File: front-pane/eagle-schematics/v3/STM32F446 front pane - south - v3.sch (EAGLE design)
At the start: 435 parts, among them IC1 NEOPIXEL-TLC59731DR, IC10 NEOPIXEL-TLC59731DR, IC11 NEOPIXEL-TLC59731DR, IC12 NEOPIXEL-TLC59731DR, IC13 NEOPIXEL-TLC59731DR, IC14 NEOPIXEL-TLC59731DR, IC15 NEOPIXEL-TLC59731DR, IC16 NEOPIXEL-TLC59731DR, IC17 NEOPIXEL-TLC59731DR, IC18 NEOPIXEL-TLC59731DR, IC19 NEOPIXEL-TLC59731DR, IC2 NEOPIXEL-TLC59731DR, IC20 NEOPIXEL-TLC59731DR, IC21 NEOPIXEL-TLC59731DR, IC22 NEOPIXEL-TLC59731DR, IC23 NEOPIXEL-TLC59731DR, IC24 NEOPIXEL-TLC59731DR, IC25 NEOPIXEL-TLC59731DR, IC26 NEOPIXEL-TLC59731DR, IC27 NEOPIXEL-TLC59731DR, IC28 NEOPIXEL-TLC59731DR, IC29 NEOPIXEL-TLC59731DR, IC3 NEOPIXEL-TLC59731DR, IC30 NEOPIXEL-TLC59731DR, IC31 NEOPIXEL-TLC59731DR, IC32 NEOPIXEL-TLC59731DR, IC33 NEOPIXEL-TLC59731DR, IC4 NEOPIXEL-TLC59731DR, IC5 NEOPIXEL-TLC59731DR, IC6 NEOPIXEL-TLC59731DR, IC7 NEOPIXEL-TLC59731DR, IC8 NEOPIXEL-TLC59731DR, IC9 NEOPIXEL-TLC59731DR, SW1 B3F-1000, SW10 B3F-1000, SW2 B3F-1000, SW3 B3F-1000, SW4 B3F-1000, SW5 B3F-1000, SW6 B3F-1000, SW7 B3F-1000, SW8 B3F-1000, SW9 B3F-1000

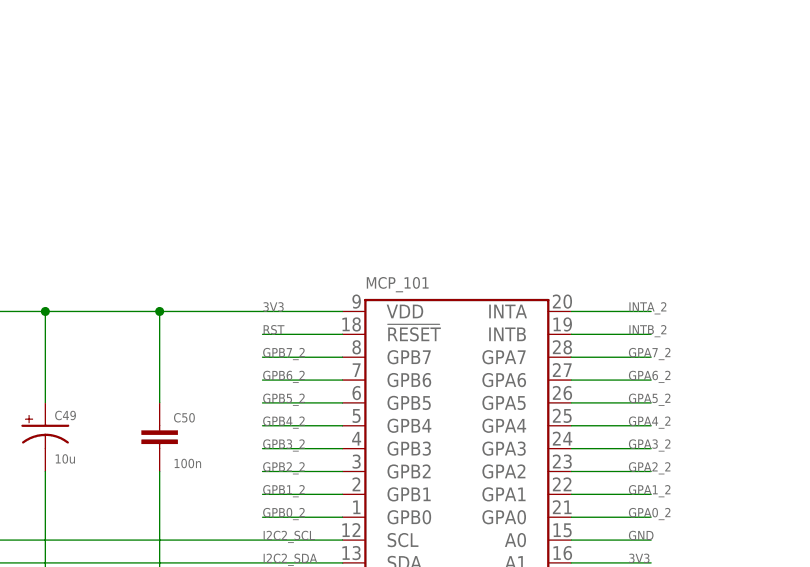
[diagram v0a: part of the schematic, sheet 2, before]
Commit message: Fixed bug with MCP_XXX name
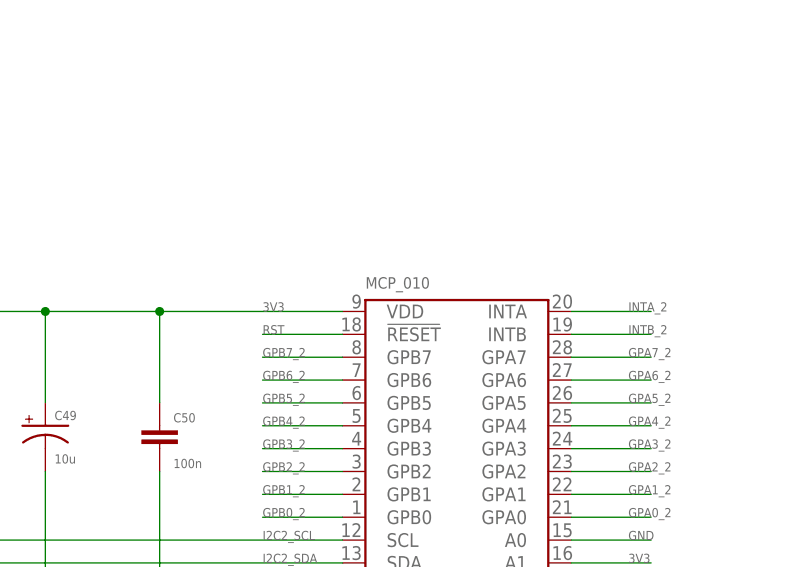
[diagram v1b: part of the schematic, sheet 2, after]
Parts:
- renumbered MCP_101 to MCP_010
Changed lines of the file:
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@@
 <part name="C75" library="stock-perso" deviceset="PASSIF-CAP" device="-0805" value="100n"/>
 <part name="C79" library="stock-perso" deviceset="PASSIF-CPOL-US" device="2917" value="10u"/>
-<part name="MCP_101" library="a_ranger_work" deviceset="MCP23017" device=""/>
+<part name="MCP_010" library="a_ranger_work" deviceset="MCP23017" device=""/>
 <part name="C49" library="stock-perso" deviceset="PASSIF-CPOL-US" device="2917" value="10u"/>
 <part name="C50" library="stock-perso" deviceset="PASSIF-CAP" device="-0805" value="100n"/>
@@
 <attribute name="VALUE" x="368.046" y="275.209" size="1.778" layer="96"/>
 </instance>
-<instance part="MCP_101" gate="G$1" x="-78.74" y="189.23" smashed="yes">
+<instance part="MCP_010" gate="G$1" x="-78.74" y="189.23" smashed="yes">
 <attribute name="NAME" x="-88.9" y="205.74" size="1.27" layer="95" ratio="12"/>
 <attribute name="VALUE" x="-88.9" y="168.91" size="1.27" layer="96" ratio="12"/>
@@
 </segment>
 <segment>
-<pinref part="MCP_101" gate="G$1" pin="VSS"/>
+<pinref part="MCP_010" gate="G$1" pin="VSS"/>
 <label x="-100.33" y="172.72" size="1.016" layer="95"/>
 <pinref part="C49" gate="G$1" pin="-"/>
@@
 <segment>
 <wire x1="-66.04" y1="172.72" x2="-57.15" y2="172.72" width="0.1524" layer="91"/>
-<pinref part="MCP_101" gate="G$1" pin="A2"/>
+<pinref part="MCP_010" gate="G$1" pin="A2"/>
 <label x="-59.69" y="172.72" size="1.016" layer="95"/>
 </segment>
 <segment>
 <wire x1="-66.04" y1="177.8" x2="-57.15" y2="177.8" width="0.1524" layer="91"/>
-<pinref part="MCP_101" gate="G$1" pin="A0"/>
+<pinref part="MCP_010" gate="G$1" pin="A0"/>
 <label x="-59.69" y="177.8" size="1.016" layer="95"/>
 </segment>
@@
 </segment>
 <segment>
-<pinref part="MCP_101" gate="G$1" pin="VDD"/>
+<pinref part="MCP_010" gate="G$1" pin="VDD"/>
 <label x="-100.33" y="203.2" size="1.016" layer="95"/>
 <wire x1="-91.44" y1="203.2" x2="-111.76" y2="203.2" width="0.1524" layer="91"/>
@@
 <segment>
 <wire x1="-66.04" y1="175.26" x2="-57.15" y2="175.26" width="0.1524" layer="91"/>
-<pinref part="MCP_101" gate="G$1" pin="A1"/>
+<pinref part="MCP_010" gate="G$1" pin="A1"/>
 <label x="-59.69" y="175.26" size="1.016" layer="95"/>
 </segment>
@@
 <segment>
 <wire x1="-100.33" y1="200.66" x2="-91.44" y2="200.66" width="0.1524" layer="91"/>
-<pinref part="MCP_101" gate="G$1" pin="!RESET"/>
+<pinref part="MCP_010" gate="G$1" pin="!RESET"/>
 <label x="-100.33" y="200.66" size="1.016" layer="95"/>
 </segment>
@@
 <segment>
 <wire x1="-100.33" y1="198.12" x2="-91.44" y2="198.12" width="0.1524" layer="91"/>
-<pinref part="MCP_101" gate="G$1" pin="GPB7"/>
+<pinref part="MCP_010" gate="G$1" pin="GPB7"/>
 <label x="-100.33" y="198.12" size="1.016" layer="95"/>
 </segment>
@@
 <segment>
 <wire x1="-100.33" y1="195.58" x2="-91.44" y2="195.58" width="0.1524" layer="91"/>
-<pinref part="MCP_101" gate="G$1" pin="GPB6"/>
+<pinref part="MCP_010" gate="G$1" pin="GPB6"/>
 <label x="-100.33" y="195.58" size="1.016" layer="95"/>
 </segment>
@@
 <segment>
 <wire x1="-100.33" y1="193.04" x2="-91.44" y2="193.04" width="0.1524" layer="91"/>
-<pinref part="MCP_101" gate="G$1" pin="GPB5"/>
+<pinref part="MCP_010" gate="G$1" pin="GPB5"/>
 <label x="-100.33" y="193.04" size="1.016" layer="95"/>
 </segment>
@@
 <segment>
 <wire x1="-100.33" y1="190.5" x2="-91.44" y2="190.5" width="0.1524" layer="91"/>
-<pinref part="MCP_101" gate="G$1" pin="GPB4"/>
+<pinref part="MCP_010" gate="G$1" pin="GPB4"/>
 <label x="-100.33" y="190.5" size="1.016" layer="95"/>
 </segment>
@@
 <segment>
 <wire x1="-100.33" y1="187.96" x2="-91.44" y2="187.96" width="0.1524" layer="91"/>
-<pinref part="MCP_101" gate="G$1" pin="GPB3"/>
+<pinref part="MCP_010" gate="G$1" pin="GPB3"/>
 <label x="-100.33" y="187.96" size="1.016" layer="95"/>
 </segment>
@@
 <segment>
 <wire x1="-100.33" y1="185.42" x2="-91.44" y2="185.42" width="0.1524" layer="91"/>
-<pinref part="MCP_101" gate="G$1" pin="GPB2"/>
+<pinref part="MCP_010" gate="G$1" pin="GPB2"/>
 <label x="-100.33" y="185.42" size="1.016" layer="95"/>
 </segment>
@@
 <segment>
 <wire x1="-100.33" y1="182.88" x2="-91.44" y2="182.88" width="0.1524" layer="91"/>
-<pinref part="MCP_101" gate="G$1" pin="GPB1"/>
+<pinref part="MCP_010" gate="G$1" pin="GPB1"/>
 <label x="-100.33" y="182.88" size="1.016" layer="95"/>
 </segment>
@@
 <segment>
 <wire x1="-100.33" y1="180.34" x2="-91.44" y2="180.34" width="0.1524" layer="91"/>
-<pinref part="MCP_101" gate="G$1" pin="GPB0"/>
+<pinref part="MCP_010" gate="G$1" pin="GPB0"/>
 <label x="-100.33" y="180.34" size="1.016" layer="95"/>
 </segment>
@@
 <segment>
 <wire x1="-66.04" y1="180.34" x2="-57.15" y2="180.34" width="0.1524" layer="91"/>
-<pinref part="MCP_101" gate="G$1" pin="GPA0"/>
+<pinref part="MCP_010" gate="G$1" pin="GPA0"/>
 <label x="-59.69" y="180.34" size="1.016" layer="95"/>
 </segment>
@@
 <segment>
 <wire x1="-66.04" y1="182.88" x2="-57.15" y2="182.88" width="0.1524" layer="91"/>
-<pinref part="MCP_101" gate="G$1" pin="GPA1"/>
+<pinref part="MCP_010" gate="G$1" pin="GPA1"/>
 <label x="-59.69" y="182.88" size="1.016" layer="95"/>
 </segment>
@@
 <segment>
 <wire x1="-66.04" y1="185.42" x2="-57.15" y2="185.42" width="0.1524" layer="91"/>
-<pinref part="MCP_101" gate="G$1" pin="GPA2"/>
+<pinref part="MCP_010" gate="G$1" pin="GPA2"/>
 <label x="-59.69" y="185.42" size="1.016" layer="95"/>
 </segment>
@@
 <segment>
 <wire x1="-66.04" y1="187.96" x2="-57.15" y2="187.96" width="0.1524" layer="91"/>
-<pinref part="MCP_101" gate="G$1" pin="GPA3"/>
+<pinref part="MCP_010" gate="G$1" pin="GPA3"/>
 <label x="-59.69" y="187.96" size="1.016" layer="95"/>
 </segment>
@@
 <segment>
 <wire x1="-66.04" y1="190.5" x2="-57.15" y2="190.5" width="0.1524" layer="91"/>
-<pinref part="MCP_101" gate="G$1" pin="GPA4"/>
+<pinref part="MCP_010" gate="G$1" pin="GPA4"/>
 <label x="-59.69" y="190.5" size="1.016" layer="95"/>
 </segment>
@@
 <segment>
 <wire x1="-66.04" y1="193.04" x2="-57.15" y2="193.04" width="0.1524" layer="91"/>
-<pinref part="MCP_101" gate="G$1" pin="GPA5"/>
+<pinref part="MCP_010" gate="G$1" pin="GPA5"/>
 <label x="-59.69" y="193.04" size="1.016" layer="95"/>
 </segment>
@@
 <segment>
 <wire x1="-66.04" y1="195.58" x2="-57.15" y2="195.58" width="0.1524" layer="91"/>
-<pinref part="MCP_101" gate="G$1" pin="GPA6"/>
+<pinref part="MCP_010" gate="G$1" pin="GPA6"/>
 <label x="-59.69" y="195.58" size="1.016" layer="95"/>
 </segment>
@@
 <segment>
 <wire x1="-66.04" y1="198.12" x2="-57.15" y2="198.12" width="0.1524" layer="91"/>
-<pinref part="MCP_101" gate="G$1" pin="GPA7"/>
+<pinref part="MCP_010" gate="G$1" pin="GPA7"/>
 <label x="-59.69" y="198.12" size="1.016" layer="95"/>
 </segment>
@@
 <segment>
 <wire x1="-66.04" y1="203.2" x2="-57.15" y2="203.2" width="0.1524" layer="91"/>
-<pinref part="MCP_101" gate="G$1" pin="INTA"/>
+<pinref part="MCP_010" gate="G$1" pin="INTA"/>
 <label x="-59.69" y="203.2" size="1.016" layer="95"/>
 </segment>
@@
 <segment>
 <wire x1="-66.04" y1="200.66" x2="-57.15" y2="200.66" width="0.1524" layer="91"/>
-<pinref part="MCP_101" gate="G$1" pin="INTB"/>
+<pinref part="MCP_010" gate="G$1" pin="INTB"/>
 <label x="-59.69" y="200.66" size="1.016" layer="95"/>
 </segment>
@@
 <segment>
 <pinref part="R85" gate="G$1" pin="1"/>
-<pinref part="MCP_101" gate="G$1" pin="SCL"/>
+<pinref part="MCP_010" gate="G$1" pin="SCL"/>
 <label x="-100.33" y="177.8" size="1.016" layer="95"/>
 <wire x1="-137.16" y1="177.8" x2="-91.44" y2="177.8" width="0.1524" layer="91"/>
@@
 <pinref part="R84" gate="G$1" pin="1"/>
 <wire x1="-144.78" y1="175.26" x2="-91.44" y2="175.26" width="0.1524" layer="91"/>
-<pinref part="MCP_101" gate="G$1" pin="SDA"/>
+<pinref part="MCP_010" gate="G$1" pin="SDA"/>
 <label x="-100.33" y="175.26" size="1.016" layer="95"/>
 </segment>
